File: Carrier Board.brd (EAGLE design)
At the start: 88 x 34.9 mm, 57 parts, among them J4 S2B-PH-SM4-TB(LF)(SN), J5 S2B-PH-SM4-TB(LF)(SN), Q1 MMBT2222A, U1 TMP36GRTZ, U2 TPL5010, U3 MB85RC256, U4 Particle Electron, U5 TPS22810, U6 TPS22810, U7 NAND

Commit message: v0.1 - First rough layout
Just getting started.
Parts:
- removed C6, C7: 0.1uF, SparkFun-Capacitors:0805@1
- removed J1, J2/SPI: (no value), SparkFun-Connectors:2X3
- removed R8, R9: 100, SparkFun-Passives:0805
- removed U4: Particle Electron, Particle-Devices:ELECTON-PWR-PINS
- removed U5, U6: TPS22810, Custom Components:SOT-23-6
- added BORON: PARTICLE-DEVICES-BORON, Carrier Board:PARTICLE-DEVICES_BORON
- added JP8: (no value), SparkFun-Connectors:1X06_LOCK
- moved J3 31.2 mm to (13.7, 3.10), turned to 0 degrees
- moved JP1 29.3 mm to (45.1, 3.28)
- moved R7 19.9 mm to (19.8, 16.4)
- moved R6 19.6 mm to (17.1, 16.5)
- moved U3 19.5 mm to (11.4, 15.4)
- moved G1 16.0 mm to (17.4, 11.7)
- moved R3 8.44 mm to (41.2, 13.2)
- moved C1 2.99 mm to (27.7, 13.5)
- moved R12 2.75 mm to (51.4, 23.3)
- moved D1 2.41 mm to (69.6, 17.0)
- moved C5 2.40 mm to (51.4, 19.3)
- moved FD2 2.38 mm to (0.97, 5.49)
- moved Q1 2.17 mm to (47.9, 20.2)
- moved R10 2.02 mm to (44.9, 22.2)
- moved U2 1.87 mm to (36.9, 13.0)
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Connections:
- removed net A4: J2/SPI.3, U4.8
- removed net B0: U4.18
- removed net B1: J1.1, U4.17
- removed net B2: J1.3, U4.16
- removed net B3: J1.5, U4.15
- removed net B4: J1.4, U4.14
- removed net BATT-IN: D2.ANODE, J5.2, U6.1
- removed net C0: U4.19
- removed net C1: U4.20
- removed net C2: JP2.2, U4.21
- removed net C3: JP2.3, U4.22
- removed net C4: JP2.4, U4.23
- removed net C5: JP2.5, U4.24
- removed net DAC: U4.6
- removed net DC-IN: C8.P$1, D3.ANODE, F1.2, U5.1, V1.2
- removed net N$2: C6.1, U5.4
- removed net N$5: C7.1, U6.4
- removed net N$6: R8.1, U6.5
- removed net N$7: R9.1, U5.5
- removed net ON/OFF: U5.3, U6.3, U7.3
- removed net VBAT: U4.34
- removed net VIN: R9.2, U4.1, U5.6
- new net 3V3: BORON.3V3
- new net A0: BORON.A0, JP8.5
- new net D7: BORON.D7
- new net EN: BORON.EN, U7.3
- new net MD: BORON.MD
- new net MISO: BORON.MI, JP2.3
- new net MOSI: BORON.MO, JP2.4
- new net SCK: BORON.SCK, JP2.5
- new net VUSB: BORON.VUSB, C8.P$1, D3.ANODE, F1.2, V1.2
- new net WAKE: BORON.D6
- net !RST: now also BORON.RST; no longer U4.35
- net !SHTDWN: now also BORON.D8; no longer U4.13
- net A1: now also BORON.A1, JP8.4; no longer U4.11
- net A2: now also BORON.A2, JP8.3; no longer J2/SPI.4, U4.10
- net A3: now also BORON.A3, JP8.2; no longer J2/SPI.1, U4.9
- net A5: now also BORON.A5, JP2.2; no longer J2/SPI.5, U4.7
- net D2: now also BORON.D2; no longer U4.27
- net D3: now also BORON.D3; no longer U4.28
- net DONE: now also BORON.D5; no longer U4.31
- net GND: now also BORON.GND, JP8.1; no longer C6.2, C7.2, J1.6, J2/SPI.6, U4.2, U4.33, U5.2, U6.2
- net HARD-RESET: no longer U4.29
- net LI+: now also BORON.LI+, D2.ANODE, J5.2; no longer R8.2, U4.LI+, U6.6
- net RX: now also BORON.RX; no longer U4.4
- net SCL: now also BORON.SCL; no longer U4.26
- net SDA: now also BORON.SDA; no longer U4.25
- net TEMP: now also BORON.A4; no longer U4.12
- net TX: now also BORON.TX; no longer U4.3
- net USER-SW: now also BORON.D4; no longer U4.30
- net VCC: now also JP8.6; no longer J1.2, J2/SPI.2, JP2.6, U4.36
- net VCC-EXT: now also JP2.6
- net WKP: no longer U4.5
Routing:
- net VCC: track 175.1 -> 0.00 mm
- net DC-IN: track 47.0 -> 0.00 mm, vias 1 -> 0
- net SCL: track 38.0 -> 0.00 mm
- net ENABLE-PWR: track 37.2 -> 0.00 mm
- net ON/OFF: track 35.2 -> 0.00 mm
- net SDA: track 33.8 -> 0.00 mm
- net !HARD-RESET: track 31.0 -> 0.00 mm, vias 2 -> 0
- net N$25: track 22.5 -> 0.00 mm, vias 1 -> 0
- net !RST: track 21.8 -> 0.00 mm
- net BATT-IN: track 19.8 -> 0.00 mm, vias 1 -> 0
- net N$24: track 18.7 -> 0.00 mm
- net D2: track 17.5 -> 0.00 mm
- net D3: track 16.8 -> 0.00 mm
- net DONE: track 15.7 -> 0.00 mm
- net HARD-RESET: track 13.3 -> 0.00 mm, vias 1 -> 0
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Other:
- board size 88 x 34.9 mm -> 90.4 x 36.1 mm

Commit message: v0.1a - updated readme
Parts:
- moved C3 5.96 mm to (36.7, 23.8)
- moved R4 5.86 mm to (42.0, 23.8)
- moved R5 5.85 mm to (39.5, 23.8)
- moved Q1 1.73 mm to (47.8, 21.9)
- moved V3 1.70 mm to (24.8, 33.4)
- moved R10 1.57 mm to (44.6, 23.7)
- moved F3 1.56 mm to (27.7, 32.4)
- moved R12 1.37 mm to (51.4, 21.9)
- moved C5 0.56 mm to (51.4, 18.7)

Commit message: v0.11 - Refining placments
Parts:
- removed S1: B3F-1070, switch-omron:B3F-10XX
- added SW2: MF-SW-TACT-6MM, MF_Switches:TACT6MM
- moved JP1 37.9 mm to (21.4, 32.9)
- moved JP2 29.9 mm to (14.6, 2.92)
- moved JP8 29.3 mm to (33.4, 2.97)
- moved R3 23.9 mm to (19.1, 22.2), turned to 270 degrees
- moved BORON 22.5 mm to (1.78, 6.22), flipped to the bottom, turned to 90 degrees
- moved U2 17.8 mm to (21.7, 22.3), turned to 90 degrees
- moved R7 17.2 mm to (3.68, 22.6), turned to 270 degrees
- moved C1 16.6 mm to (11.7, 17.6), turned to 0 degrees
- moved R6 12.8 mm to (5.87, 22.6), turned to 270 degrees
- moved R2 12.6 mm to (24.4, 22.3)
- moved R1 12.4 mm to (26.1, 22.3)
- moved U1 12.3 mm to (31.8, 22.1), turned to 90 degrees
- moved U3 6.81 mm to (11.5, 22.2)
- moved J5 5.13 mm to (67.8, 32.3)
- moved J3 3.66 mm to (10.1, 3.00)
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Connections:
- removed net WKP: U2.5
- net GND: now also SW2.P$3, SW2.P$4; no longer S1.3, S1.4
- net N$4: now also SW2.P$1, SW2.P$2; no longer S1.1, S1.2
- net WAKE: now also U2.5
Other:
- board size 90.4 x 36.1 mm -> 90 x 36.1 mm

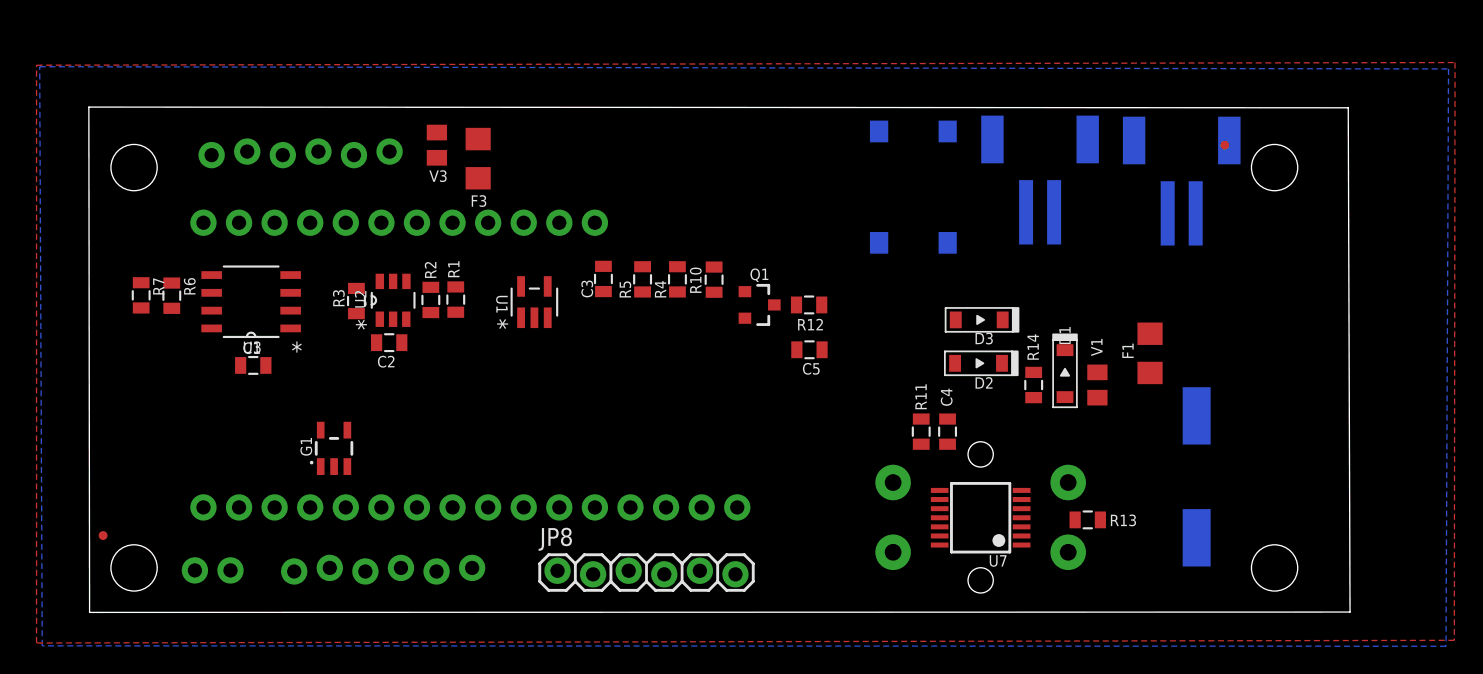
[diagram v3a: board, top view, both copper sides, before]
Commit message: More tweaks
D8 for wake, no shutdown on TMP-36 and Hard-reset connected.  Power protection for off-board VCC
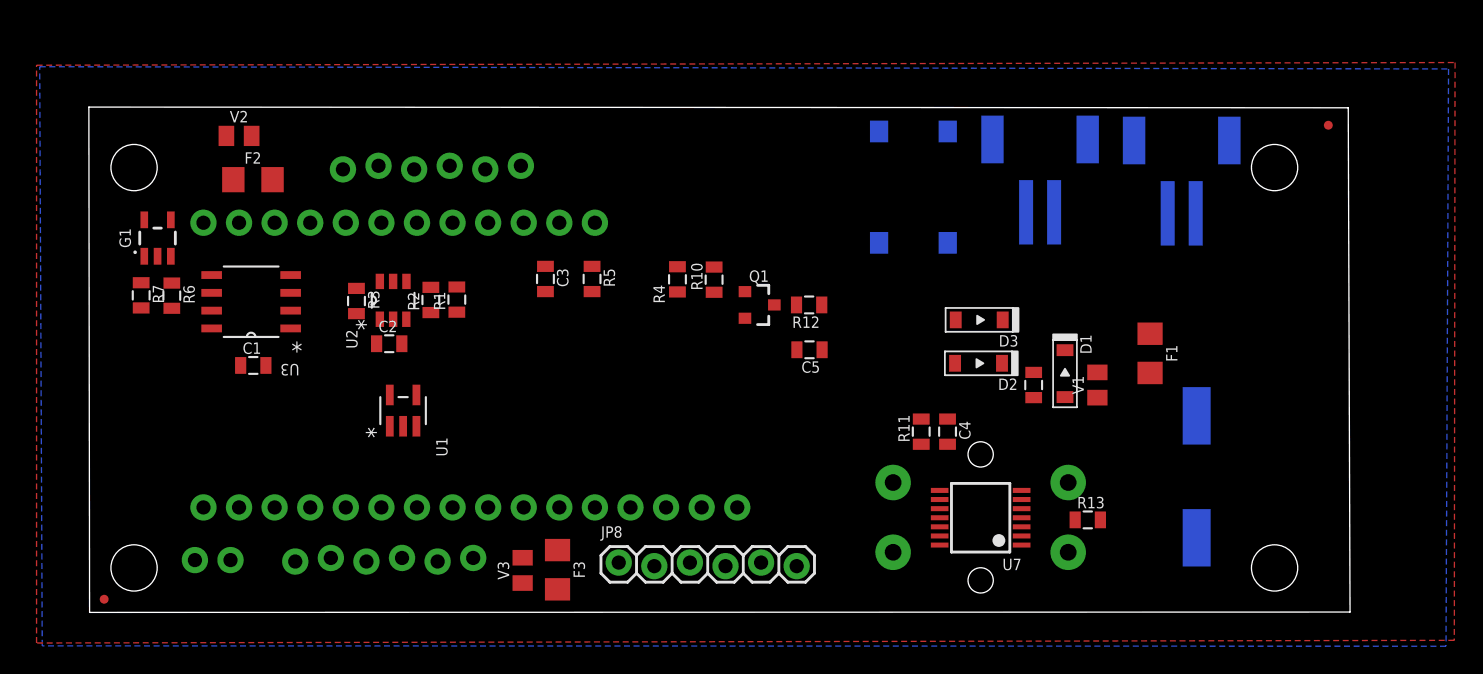
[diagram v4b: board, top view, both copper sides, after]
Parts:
- added F2: 500mA - FAST BLOW, SparkFun-Fuses:1206
- added V2: VC080505C150DP, Custom Components:0805
- moved V3 31.0 mm to (30.9, 3.00), turned to 90 degrees
- moved F3 29.9 mm to (33.4, 3.05), turned to 270 degrees
- moved G1 19.6 mm to (4.85, 26.7)
- moved U1 12.2 mm to (22.4, 14.4)
- moved JP1 9.43 mm to (30.8, 31.9)
- moved FD1 7.53 mm to (88.4, 34.8)
- moved FD2 4.55 mm to (1.04, 0.94)
- moved JP8 4.41 mm to (37.8, 3.56)
- moved C3 4.14 mm to (32.5, 23.8)
- moved R5 3.61 mm to (35.9, 23.8)
- moved J3 0.74 mm to (10.1, 3.73)
- moved JP2 0.72 mm to (14.7, 3.63)
- moved C2 0.08 mm to (21.4, 19.2)
- moved R1 0.08 mm to (26.2, 22.3)
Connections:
- net A5 renamed SS
- removed net !SHTDWN: BORON.D8, U1.4
- new net VCC2-EXT: F2.2, JP1.6, V2.2
- net GND: now also JP8.6, V2.1; no longer JP8.1
- net HARD-RESET: now also BORON.D6
- net VCC: now also F2.1, U1.4; no longer JP8.6
- net VCC-EXT: now also JP8.1; no longer JP1.6
- net WAKE: now also BORON.D8; no longer BORON.D6

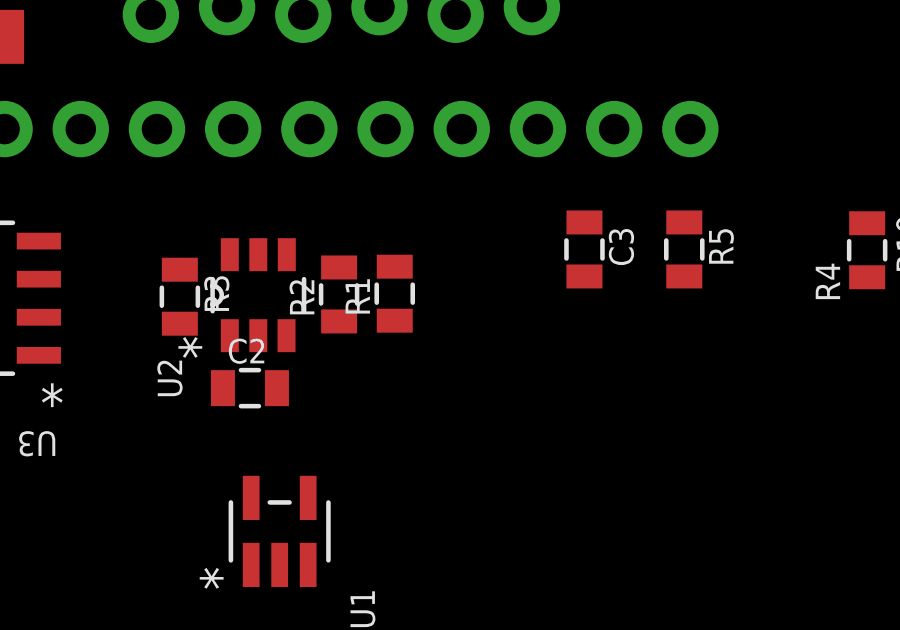
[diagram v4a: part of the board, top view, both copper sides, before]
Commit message: Added Heratch's v3 starter
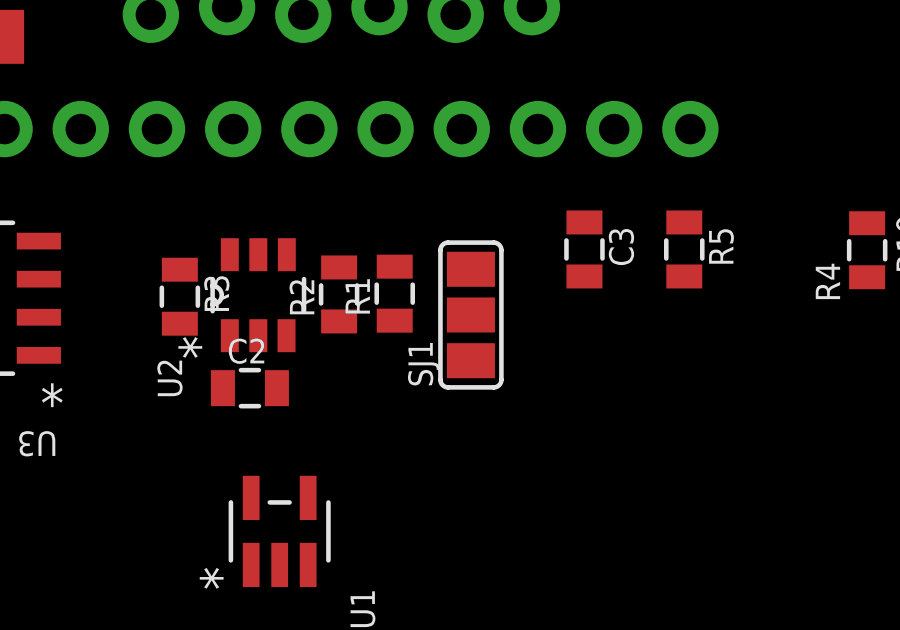
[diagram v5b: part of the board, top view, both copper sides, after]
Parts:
- added SJ1: (no value), jumper:SJ_2
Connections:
- new net RESET: R3.1, SJ1.2, U2.6
- net !RST: now also SJ1.1; no longer R3.1, U2.6
- net EN: now also SJ1.3
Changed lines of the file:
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@@
 <attribute name="PROD_ID" value="RES-08585" x="11.6586" y="30.8864" size="1.778" layer="27" display="off"/>
+</element>
+<element name="SJ1" library="jumper" library_urn="urn:adsk.eagle:library:252" package="SJ_2" package3d_urn="urn:adsk.eagle:package:15474/1" value="" x="28.7528" y="21.6154" smashed="yes" rot="R90">
+<attribute name="NAME" x="27.4828" y="19.2024" size="0.8128" layer="25" ratio="10" rot="R90"/>
+<attribute name="VALUE" x="28.7528" y="21.5153" size="0.02" layer="27" rot="R90"/>
 </element>
 </elements>
@@
 </signal>
 <signal name="!RST">
-<contactref element="R3" pad="1"/>
-<contactref element="U2" pad="6"/>
 <contactref element="BORON" pad="RST"/>
-<wire x1="19.05" y1="23.125" x2="46.228" y2="7.493" width="0" layer="19" extent="1-1"/>
-<wire x1="20.7162" y1="23.6258" x2="19.05" y2="23.125" width="0" layer="19" extent="1-1"/>
+<contactref element="SJ1" pad="1"/>
+<wire x1="28.7528" y1="20.0914" x2="46.228" y2="7.493" width="0" layer="19" extent="1-1"/>
 </signal>
 <signal name="HARD-RESET">
@@
 <contactref element="BORON" pad="EN"/>
 <contactref element="U7" pad="3"/>
+<contactref element="SJ1" pad="3"/>
 <wire x1="33.528" y1="27.813" x2="66.5266" y2="6.1064" width="0" layer="19" extent="1-1"/>
+<wire x1="28.7528" y1="23.1394" x2="33.528" y2="27.813" width="0" layer="19" extent="1-1"/>
 </signal>
 <signal name="VUSB">
@@
 <wire x1="18.0848" y1="31.623" x2="11.5697" y2="34.0106" width="0" layer="19" extent="1-1"/>
 </signal>
+<signal name="RESET">
+<contactref element="R3" pad="1"/>
+<contactref element="U2" pad="6"/>
+<contactref element="SJ1" pad="2"/>
+<wire x1="20.7162" y1="23.6258" x2="28.7528" y2="21.6154" width="0" layer="19" extent="1-1"/>
+<wire x1="19.05" y1="23.125" x2="20.7162" y2="23.6258" width="0" layer="19" extent="1-1"/>
+</signal>
 </signals>
 <mfgpreviewcolors>
@@
 </board>
 </drawing>
+<compatibility>
+<note version="8.2" severity="warning">
+Since Version 8.2, EAGLE supports online libraries. The ids
+of those online libraries will not be understood (or retained)
+with this version.
+</note>
+<note version="8.3" severity="warning">
+Since Version 8.3, EAGLE supports URNs for individual library
+assets (packages, symbols, and devices). The URNs of those assets
+will not be understood (or retained) with this version.
+</note>
+<note version="8.3" severity="warning">
+Since Version 8.3, EAGLE supports the association of 3D packages
+with devices in libraries, schematics, and board files. Those 3D
+packages will not be understood (or retained) with this version.
+</note>
+</compatibility>
 </eagle>

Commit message: First Pass - Ready to send to OSHPark
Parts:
- removed SJ1: (no value), jumper:SJ_2
- added JP7: JUMPER-SMT_3_1-NC_TRACE_SILK, SparkFun-Jumpers:SMT-JUMPER_3_1-NC_TRACE_SILK
- added JP9: JUMPER-SMT_2_NC_PASTE_SILK, SparkFun-Jumpers:SMT-JUMPER_2_NC_PASTE_SILK
- moved C3 19.0 mm to (49.2, 32.9)
- moved R5 18.2 mm to (51.6, 32.9)
- moved G1 16.4 mm to (20.8, 30.8), turned to 270 degrees
- moved R14 10.7 mm to (57.0, 18.8), turned to 270 degrees
- moved R4 10.3 mm to (51.6, 27.3), turned to 270 degrees
- moved D1 9.87 mm to (59.8, 18.0), turned to 90 degrees
- moved C2 9.76 mm to (15.0, 11.8), turned to 270 degrees
- moved R2 7.69 mm to (29.8, 16.9)
- moved Q1 7.65 mm to (43.4, 15.6)
- moved U2 7.56 mm to (26.8, 16.8)
- moved R1 7.55 mm to (31.4, 16.9)
- moved R10 7.41 mm to (40.6, 17.5)
- moved R3 7.31 mm to (23.9, 16.7)
- moved R12 6.34 mm to (47.0, 17.4), turned to 270 degrees
- moved R7 6.03 mm to (8.99, 25.5), turned to 180 degrees
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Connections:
- removed net 3V3: BORON.3V3
- removed net D7: BORON.D7
- new net VDD: JP9.1, U2.1
- net !RST: now also JP7.3; no longer SJ1.1
- net EN: now also JP7.1; no longer SJ1.3
- net RESET: now also JP7.2; no longer SJ1.2
- net VCC: now also BORON.3V3, JP9.2; no longer U2.1
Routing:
- net VCC: track 0.00 -> 104.7 mm
- net VUSB: track 0.00 -> 65.1 mm, vias 0 -> 2
- net EN: track 0.00 -> 47.9 mm, vias 0 -> 2
- net LI+: track 0.00 -> 42.2 mm, vias 0 -> 1
- net USER-SW: track 0.00 -> 35.8 mm
- net !HARD-RESET: track 0.00 -> 33.1 mm
- net SCL: track 0.00 -> 26.5 mm
- net N$25: track 0.00 -> 25.9 mm, vias 0 -> 1
- net ENABLE-PWR: track 0.00 -> 25.6 mm
- net HARD-RESET: track 0.00 -> 24.6 mm, vias 0 -> 1
- net SDA: track 0.00 -> 23.7 mm
- net N$24: track 0.00 -> 19.7 mm
- net D3: track 0.00 -> 19.5 mm
- net !RST: track 0.00 -> 16.9 mm, vias 0 -> 1
- net D2: track 0.00 -> 15.5 mm
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
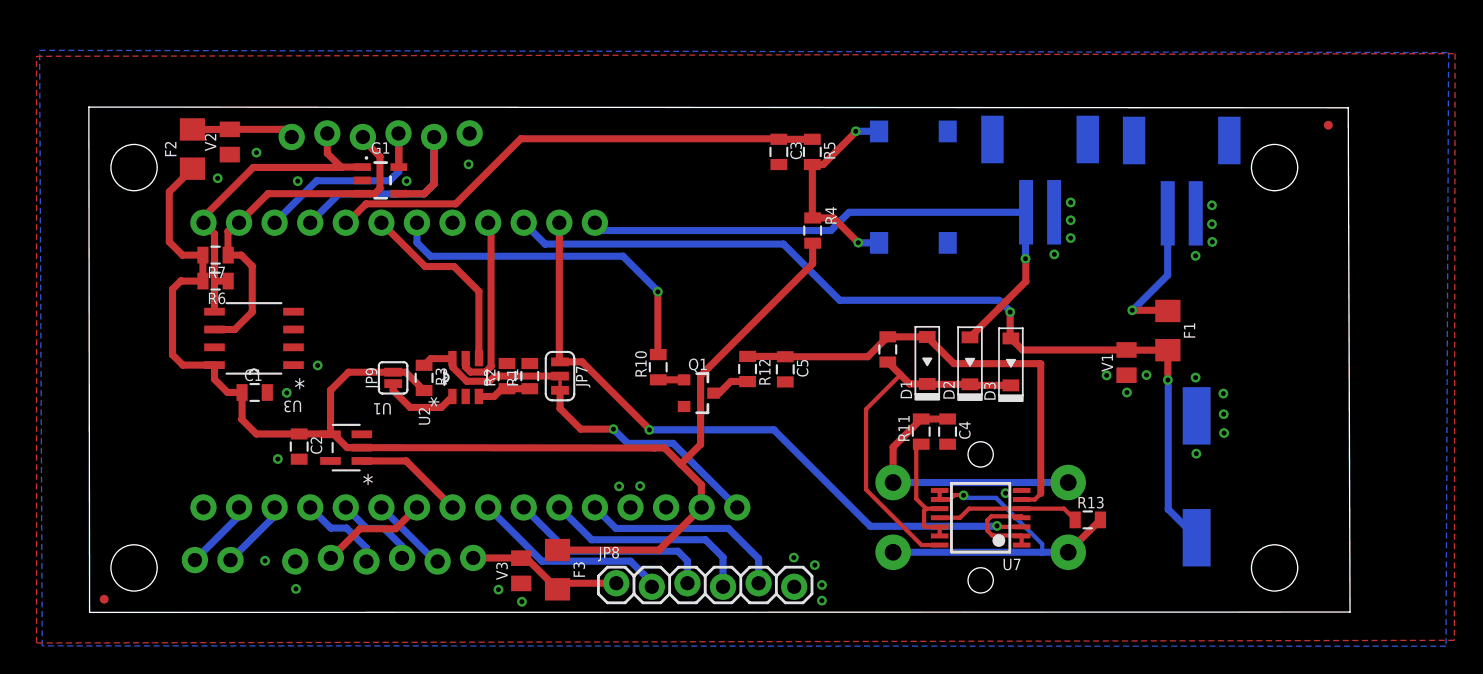
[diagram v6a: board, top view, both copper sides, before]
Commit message: Labelling and less traces under the chips
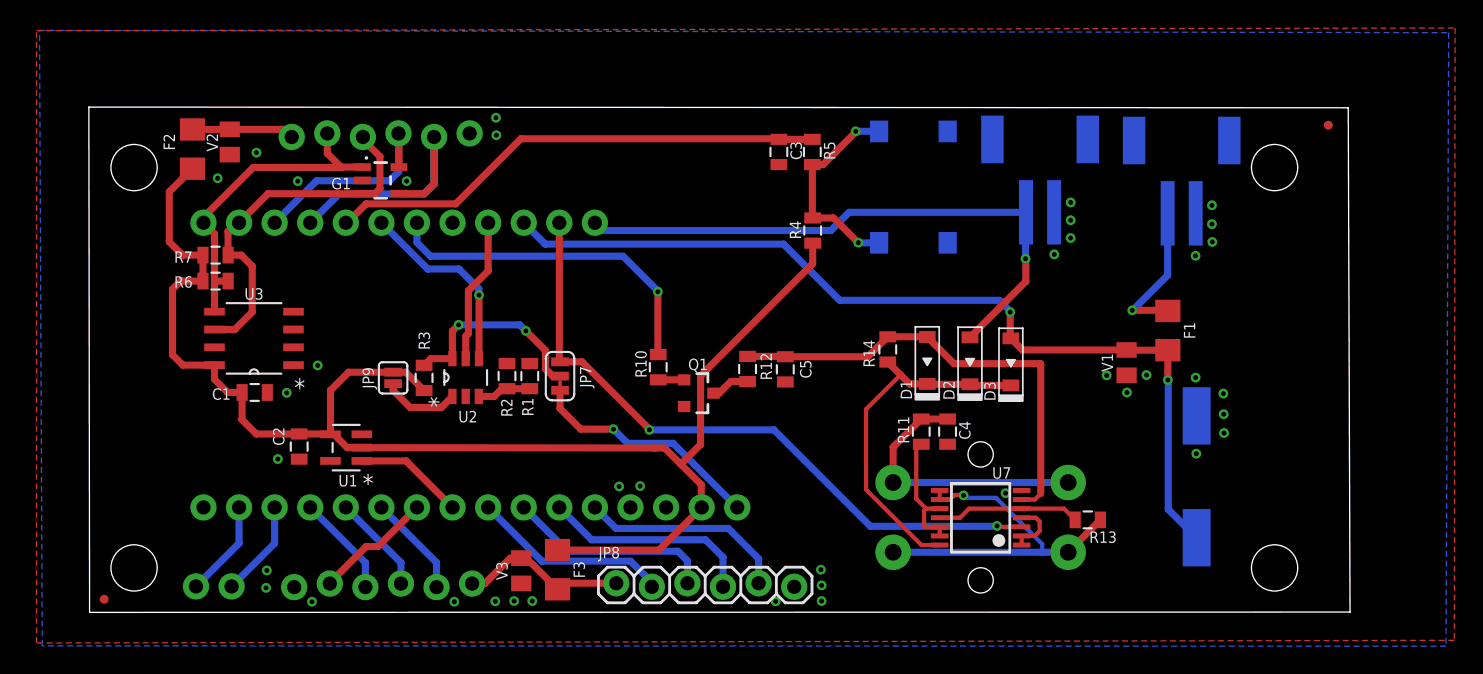
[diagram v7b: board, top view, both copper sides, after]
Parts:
- moved J3 1.88 mm to (10.1, 1.85)
- moved JP2 1.83 mm to (14.6, 1.80)
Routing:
- net RESET: track 11.1 -> 14.3 mm, vias 0 -> 2
- net WAKE: track 13.1 -> 10.4 mm
- net N$1: track 6.63 -> 4.16 mm
- net TX: track 5.06 -> 6.91 mm
- net RX: track 5.06 -> 6.91 mm
- net SCK: track 5.61 -> 7.32 mm
- net MISO: track 6.18 -> 7.32 mm
- net MOSI: track 6.00 -> 7.07 mm
- net SS: track 7.64 -> 8.50 mm
- net VCC-EXT: track 11.3 -> 12.1 mm
- net DONE: track 13.8 -> 13.9 mm, vias 0 -> 1
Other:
- board text added: "GND A0 A1 A2 A3 Vcc"
- board text added: "Rx Tx"
- board text added: "User Btn"
- board text added: "Vcc SCK MO MI SS GND"
- board text added: "v1.0- 3-29-19"
- board text removed: "A5 A4 A3"
- board text removed: "B3 B2 B1"
- board text removed: "GND A2 Vcc"
- board text removed: "GND B4 Vcc"
- board text removed: "Tx Rx"
- board text removed: "Vcc C5 C4 C3 C2 GND"
- board text removed: "v2.5 - 1-31-19"
